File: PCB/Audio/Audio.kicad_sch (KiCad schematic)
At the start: 31 parts, among them J3 TC2030-USB-NL-DS, J4 TF_PUSH, J5 USB-C-Socket-H, U1 L, U2 ESP32-S3-MINI-1, U2 R, U5 MD8942

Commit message: Closer
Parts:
- removed C6: 10uF 35V, RevK:C_0603, symbol Device:C
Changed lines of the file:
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@@
 		)
 	)
-	(global_label "DC"
-		(shape output)
-		(at 78.74 137.16 90)
-		(fields_autoplaced yes)
-		(effects
-			(font
-				(size 1.27 1.27)
-			)
-			(justify left)
-		)
-		(property "Intersheetrefs" "${INTERSHEET_REFS}"
-			(at 78.74 132.289 90)
-			(effects
-				(font
-					(size 1.27 1.27)
-				)
-				(justify left)
-				(hide yes)
-			)
-		)
-	)
 	(global_label "WS"
 		(shape input)
@@
 	)
 	(symbol
-		(lib_id "power:GND")
-		(at 78.74 144.78 0)
-		(unit 1)
-		(exclude_from_sim no)
-		(in_bom yes)
-		(on_board yes)
-		(dnp no)
-		(fields_autoplaced yes)
-		(property "Reference" "#PWR04"
-			(at 78.74 151.13 0)
-			(effects
-				(font
-					(size 1.27 1.27)
-				)
-				(hide yes)
-			)
-		)
-		(property "Value" "GND"
-			(at 78.74 149.2234 0)
-			(effects
-				(font
-					(size 1.27 1.27)
-				)
-			)
-		)
-		(property "Footprint" ""
-			(at 78.74 144.78 0)
-			(effects
-				(font
-					(size 1.27 1.27)
-				)
-				(hide yes)
-			)
-		)
-		(property "Datasheet" ""
-			(at 78.74 144.78 0)
-			(effects
-				(font
-					(size 1.27 1.27)
-				)
-				(hide yes)
-			)
-		)
-		(property "Description" "Power symbol creates a global label with name \"GND\" , ground"
-			(at 78.74 144.78 0)
-			(effects
-				(font
-					(size 1.27 1.27)
-				)
-				(hide yes)
-			)
-		)
-		(pin "1"
-		)
-		(instances
-			(project "LED"
-				(path "/46c350bb-7de4-4e81-aafd-4af55e37aab0"
-					(reference "#PWR04")
-					(unit 1)
-				)
-			)
-		)
-	)
-	(symbol
 		(lib_id "Device:C")
 		(at 38.735 140.97 0)
@@
 					(unit 1)
 				)
-			)
-		)
-	)
-	(symbol
-		(lib_id "Device:C")
-		(at 78.74 140.97 0)
-		(unit 1)
-		(exclude_from_sim no)
-		(in_bom yes)
-		(on_board yes)
-		(dnp no)
-		(property "Reference" "C6"
-			(at 82.169 139.827 0)
-			(effects
-				(font
-					(size 1.27 1.27)
-				)
-				(justify left)
-			)
-		)
-		(property "Value" "10uF 35V"
-			(at 82.169 141.859 0)
-			(effects
-				(font
-					(size 1.27 1.27)
-				)
-				(justify left)
-			)
-		)
-		(property "Footprint" "RevK:C_0603"
-			(at 79.7052 144.78 0)
-			(effects
-				(font
-					(size 1.27 1.27)
-				)
-				(hide yes)
-			)
-		)
-		(property "Datasheet" "~"
-			(at 78.74 140.97 0)
-			(effects
-				(font
-					(size 1.27 1.27)
-				)
-				(hide yes)
-			)
-		)
-		(property "Description" ""
-			(at 78.74 140.97 0)
-			(effects
-				(font
-					(size 1.27 1.27)
-				)
-				(hide yes)
-			)
-		)
-		(property "LCSC Part #" "C194427"
-			(at 78.74 140.97 0)
-			(effects
-				(font
-					(size 1.27 1.27)
-				)
-				(hide yes)
-			)
-		)
-		(pin "1"
-		)
-		(pin "2"
-		)
-		(instances
-			(project "LED"
-				(path "/46c350bb-7de4-4e81-aafd-4af55e37aab0"
-					(reference "C6")
-					(unit 1)
-				)

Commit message: Rework concept
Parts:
- removed C6: 10uF 35V, RevK:C_0603_, symbol RevK:Hidden
- removed C7: 10uF 6.3V, RevK:C_0603_, symbol RevK:Hidden
- removed C8: 100nF, RevK:C_0603_, symbol RevK:Hidden
- removed L2: 10uH, RevK:L_4x4_, symbol RevK:Hidden
- removed R10: 39k2, RevK:R_0402_, symbol RevK:Hidden
- removed R11: 1M, RevK:R_0402_, symbol RevK:Hidden
- removed R9: 124k, RevK:R_0402_, symbol RevK:Hidden
- removed U5: MD8942, RevK:SOT-23-6-MD8942, symbol RevK:MD89420-RegBlock
- added C16: 100uF, RevK:C_0805, symbol Device:C
- added C6: 100nF, RevK:C_0402, symbol Device:C
- added D2, D4: ~, RevK:DFN1006-2L, symbol RevK:ES05D1MC10
- added D3: MBR0530, RevK:D_SOD-123, symbol Device:D_Schottky
- added D5: XL-1010RGBC-WS2812B, RevK:SMD1010, symbol RevK:WS2812B-1mm
- added J1: JST-PH-SM4-TB, RevK:JST_PH_S2B-PH-SM4-TB_1x02-1MP_P2.00mm_Horizontal, symbol Connector_Generic:Conn_01x04
- added Q2: CJ2301, RevK:SOT-23, symbol Transistor_FET:BSS83P
- added R1, R8: 10K, RevK:R_0402, symbol Device:R
- added SW1: SW_Push, RevK:TS-1092S-B3D2-G, symbol Switch:SW_Push
- added U3: TP4054, RevK:SOT-23-5, symbol RevK:TP4054
- added U4: ME6211C33M5G-N, RevK:SOT-23-5, symbol Regulator_Linear:TLV70033_SOT23-5
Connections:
- net +3V3: now also C6.1, D5.2 (+)
- net GND: now also C16.2, C6.2, D2.1, D4.2, D5.3 (-), J1.1 (Pin_1), J1.3 (Pin_3), J1.4 (Pin_4), R1.1, R8.2, SW1.1, U3.2 (VSS), U4.2 (GND)
- new net: D3.1 (K), Q2.2 (S), U4.1 (IN), U4.3 (EN)
- new net: R1.2, U3.5 (PROG)
- new net +3.3V: C16.1, U4.5 (OUT)
- new net BLINK2: D5.4 (I)
- new net BUTTON: D4.1, SW1.2
- new net CHARGING: U3.1 (STAT)
- new net VBAT: D2.2, J1.2 (Pin_2), Q2.3 (D), U3.3 (VBAT)
- new net VBUS: D3.2 (A), Q2.1 (G), R8.1, U3.4 (VDD)

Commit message: Initial tracking
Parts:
- removed C7: 10uF 35V, RevK:C_0603, symbol Device:C
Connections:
- net +3.3V is gone; now on net +3V3: C16.1, U4.5 (OUT)
- net DC is gone; now on net VBUS: C5.1, J3.1 (VBUS), J3.2 (VBUS), J5.A4 (VBUS), J5.A9 (VBUS), J5.B4 (VBUS), J5.B9 (VBUS)
- net SPWR is gone; now on net +3V3: J4.4 (VDD)
- net BLINK2: now also U2.7 (GPIO3)
- net BUTTON: now also U2.33 (GPIO37)
- net CHARGING: now also U2.40 (GPIO44)
- net SCK: now also U2.15 (GPIO11); no longer U2.38 (GPIO42)
- net SD: now also U2.5 (GPIO1); no longer U2.36 (GPIO40)
- net SDCD: now also U2.21 (GPIO17)
- net SDMISO: now also U2.20 (GPIO16)
- net SDMOSI: now also U2.17 (GPIO13)
- net SDSCK: now also U2.19 (GPIO15)
- net SDSS: now also U2.16 (GPIO12)
- net WS: now also U2.4 (GPIO0); no longer U2.37 (GPIO41)
- net ADC: no longer names the net of U2.12 (GPIO8)
- net LED: no longer names the net of U2.8 (GPIO4)
- net PUSH: no longer names the net of U2.10 (GPIO6)
- no-connect marks 32 -> 28

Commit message: Position
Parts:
- J4: JLCPCB Position Offset (none) -> 0,3.075
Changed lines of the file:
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@@
+			)
+		)
+		(property "JLCPCB Position Offset" "0,3.075"
+			(at 123.19 76.835 0)
+			(effects
+				(font
+					(size 1.27 1.27)
+				)
+				(hide yes)
 			)
 		)

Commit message: Tidy
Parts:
- removed C5: 10uF 35V, RevK:C_0603, symbol Device:C
- added C11, C7: 10uF 6.3V, RevK:C_0402, symbol Device:C
- U1: value L -> R
- U2: value R -> L
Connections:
- net +3V3: now also U1.2 (LR); no longer U2.2 (LR)
- net GND: now also U2.2 (LR), C11.2, C7.2; no longer U1.2 (LR)
- net VBAT: now also C7.1
- net VBUS: now also C11.1
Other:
- moved on the sheet: C4, C6, D4, D5, SW1

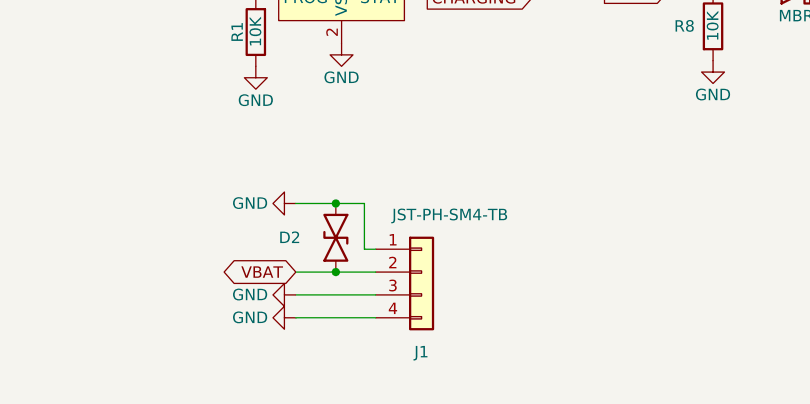
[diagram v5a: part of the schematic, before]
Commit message: DNP J1 as clashes
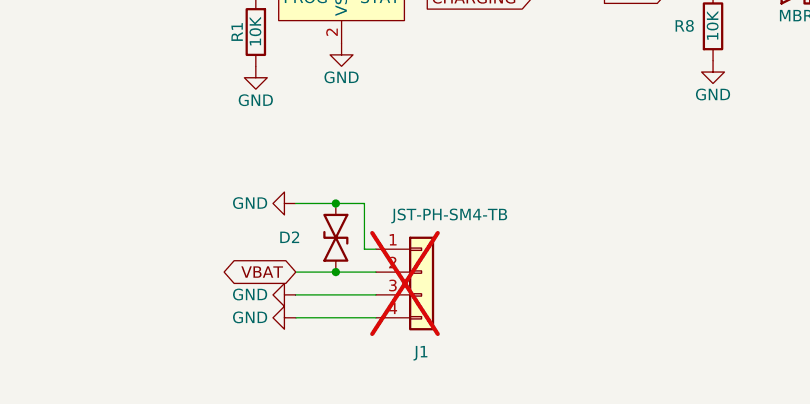
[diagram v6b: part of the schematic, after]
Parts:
- J1: now not fitted
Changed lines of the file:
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@@
 		(in_bom yes)
 		(on_board yes)
-		(dnp no)
+		(dnp yes)
 		(property "Reference" "J1"
 			(at 148.59 173.99 0)

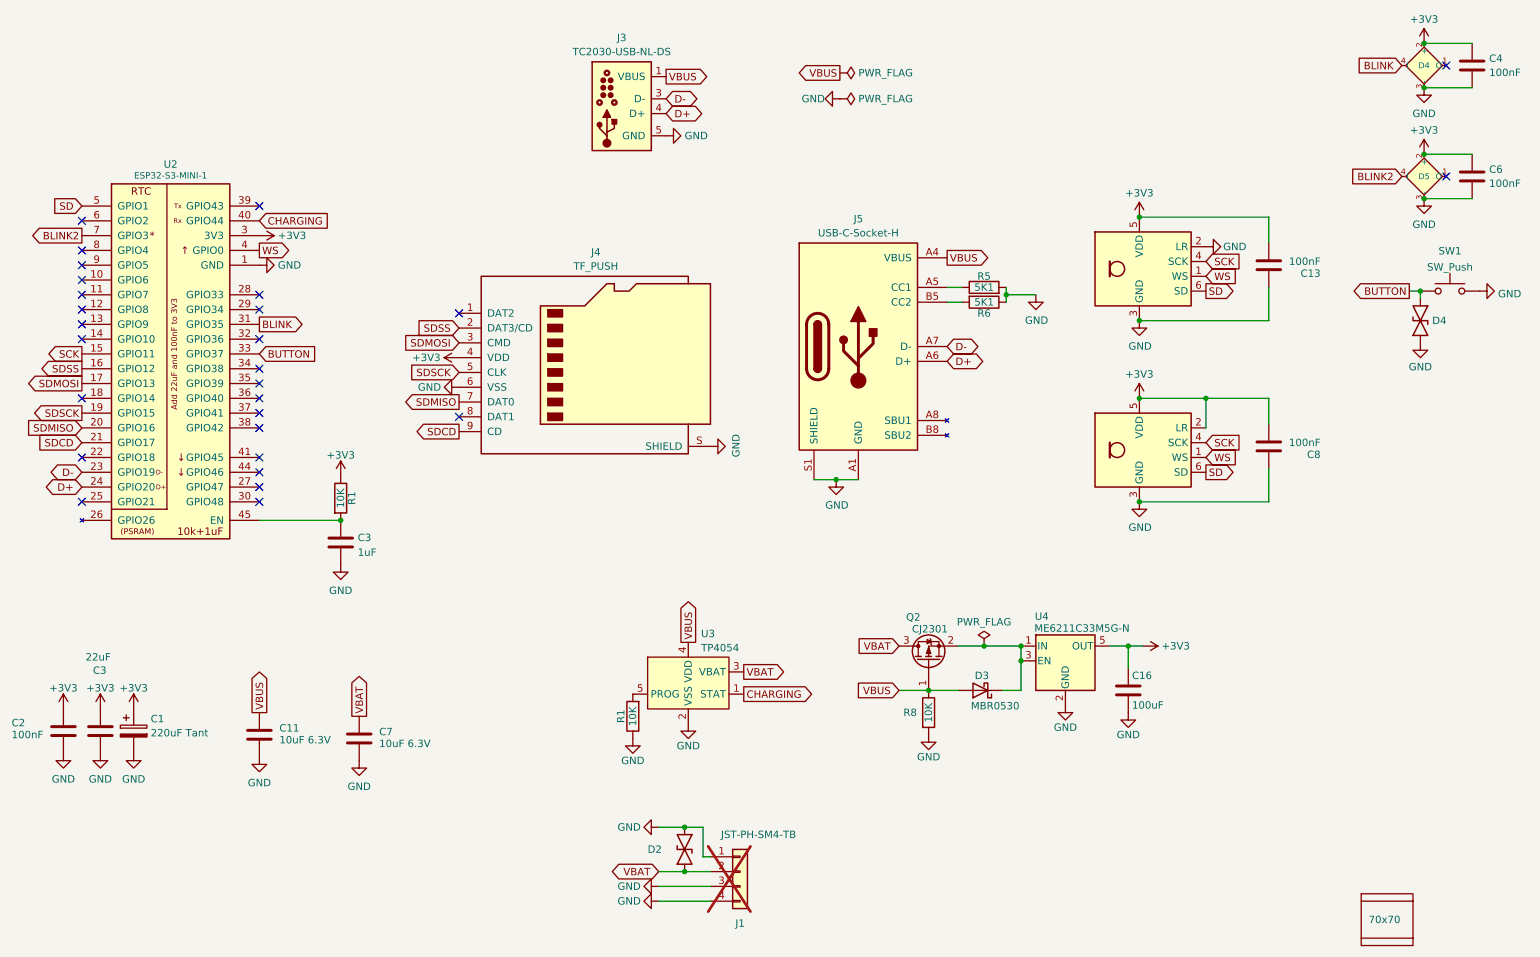
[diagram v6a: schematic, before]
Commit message: Rework, and pull ups
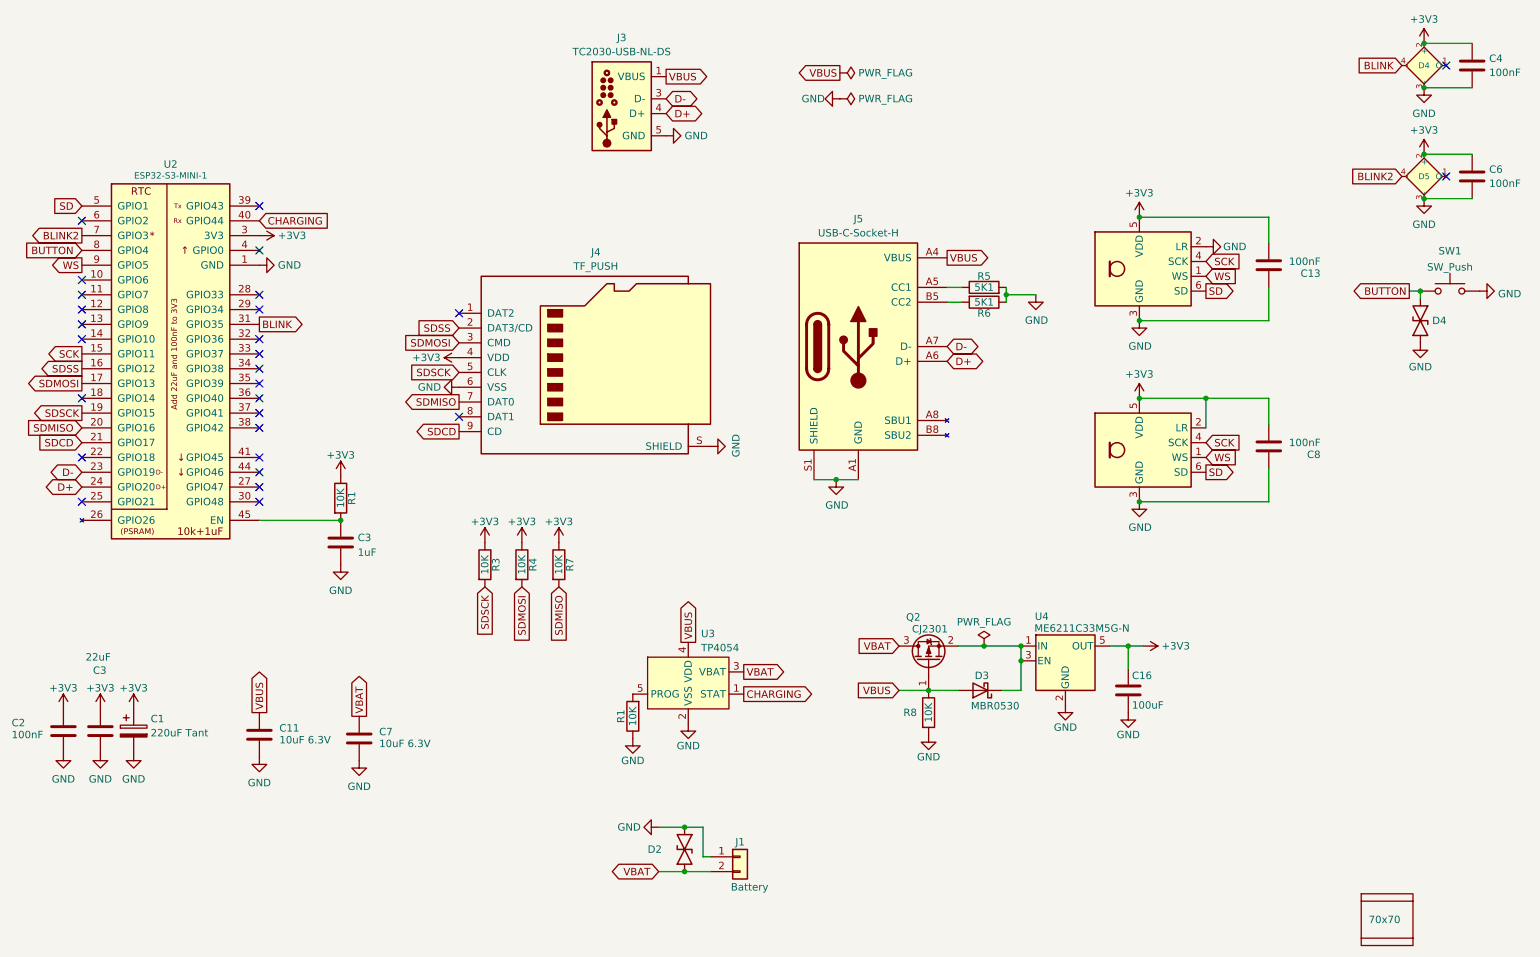
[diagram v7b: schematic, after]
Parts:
- removed J1: JST-PH-SM4-TB, RevK:JST_PH_S2B-PH-SM4-TB_1x02-1MP_P2.00mm_Horizontal, symbol Connector_Generic:Conn_01x04
- added J1: Battery, RevK:1.25T-2PWT (Molex 532610271), symbol Connector_Generic:Conn_01x02
- added R3, R4, R7: 10K, RevK:R_0402, symbol Device:R
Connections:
- net +3V3: now also R3.1, R4.1, R7.1
- net BUTTON: now also U2.8 (GPIO4); no longer U2.33 (GPIO37)
- net GND: now also J1.1 (Pin_1)
- net SDMISO: now also R7.2
- net SDMOSI: now also R4.2
- net SDSCK: now also R3.2
- net VBAT: now also J1.2 (Pin_2)
- net WS: now also U2.9 (GPIO5); no longer U2.4 (GPIO0)

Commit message: Resistors
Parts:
- removed R3, R4, R7: 10K, RevK:R_0402, symbol Device:R
- added R10, R11, R12, R13, R14, R9: 10K, RevK:R_0402, symbol Device:R
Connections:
- net +3V3: now also R10.1, R11.1, R12.1, R13.1, R14.1, R9.1
- net SDMISO: now also R10.2
- net SDMOSI: now also R12.2
- net SDSCK: now also R11.2
- net SDSS: now also R13.2
- net at J4.1 (DAT2): now also R14.2
- net at J4.8 (DAT1): now also R9.2
- no-connect marks 28 -> 26
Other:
- moved on the sheet: J4, J5, R5, R6
